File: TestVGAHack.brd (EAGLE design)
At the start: 18.3 x 7.9 mm, 0 parts

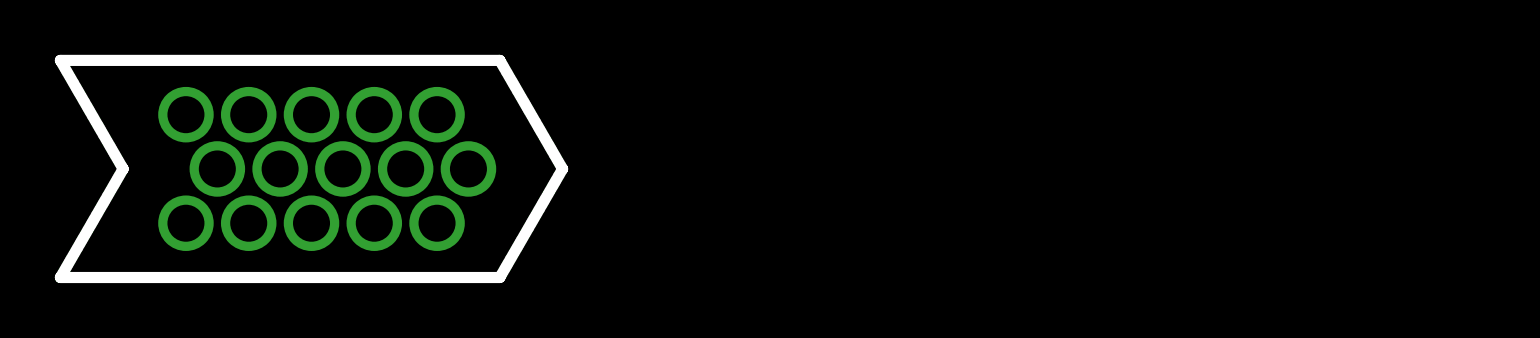
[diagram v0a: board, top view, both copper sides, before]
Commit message: Two VGA's at the same time
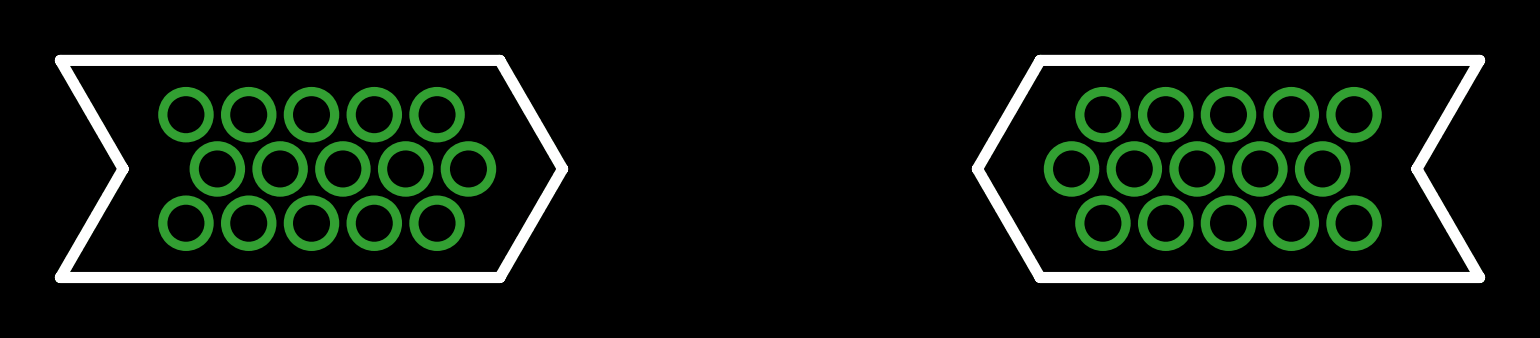
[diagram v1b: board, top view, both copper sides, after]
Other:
- board size 18.3 x 7.9 mm -> 51.8 x 7.9 mm
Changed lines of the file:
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@@
 <setting verticaltext="up"/>
 </settings>
-<grid distance="1.98" unitdist="mm" unit="mm" style="lines" multiple="1" display="yes" altdistance="1.98" altunitdist="mm" altunit="mm"/>
+<grid distance="1.145" unitdist="mm" unit="mm" style="lines" multiple="2" display="yes" altdistance="1.98" altunitdist="mm" altunit="mm"/>
 <layers>
 <layer number="1" name="Top" color="4" fill="1" visible="yes" active="yes"/>
@@
 <wire x1="-4.58" y1="1.98" x2="11.45" y2="1.98" width="0.4064" layer="20"/>
 <wire x1="-4.58" y1="-5.94" x2="11.45" y2="-5.94" width="0.4064" layer="20"/>
+<wire x1="44.9" y1="-1.98" x2="47.19" y2="-5.94" width="0.4064" layer="20"/>
+<wire x1="47.19" y1="1.98" x2="44.9" y2="-1.98" width="0.4064" layer="20"/>
+<wire x1="28.87" y1="-1.98" x2="31.16" y2="-5.94" width="0.4064" layer="20"/>
+<wire x1="31.16" y1="1.98" x2="28.87" y2="-1.98" width="0.4064" layer="20"/>
+<wire x1="47.19" y1="1.98" x2="31.16" y2="1.98" width="0.4064" layer="20"/>
+<wire x1="47.19" y1="-5.94" x2="31.16" y2="-5.94" width="0.4064" layer="20"/>
 </plain>
 <attributes>
@@
 </elements>
 <signals>
-<signal name="S$1">
+<signal name="C5">
 <via x="0" y="0" extent="1-16" drill="1.35"/>
 </signal>
-<signal name="S$2">
+<signal name="C10">
 <via x="1.145" y="-1.98" extent="1-16" drill="1.35"/>
 </signal>
-<signal name="S$3">
+<signal name="C15">
 <via x="0" y="-3.96" extent="1-16" drill="1.35"/>
 </signal>
-<signal name="S$4">
+<signal name="C4">
 <via x="2.29" y="0" extent="1-16" drill="1.35"/>
 </signal>
-<signal name="S$5">
+<signal name="C3">
 <via x="4.58" y="0" extent="1-16" drill="1.35"/>
 </signal>
-<signal name="S$6">
+<signal name="C2">
 <via x="6.87" y="0" extent="1-16" drill="1.35"/>
 </signal>
-<signal name="S$7">
+<signal name="C1">
 <via x="9.16" y="0" extent="1-16" drill="1.35"/>
 </signal>
-<signal name="S$8">
+<signal name="C14">
 <via x="2.29" y="-3.96" extent="1-16" drill="1.35"/>
 </signal>
-<signal name="S$9">
+<signal name="C13">
 <via x="4.58" y="-3.96" extent="1-16" drill="1.35"/>
 </signal>
-<signal name="S$10">
+<signal name="C12">
 <via x="6.87" y="-3.96" extent="1-16" drill="1.35"/>
 </signal>
-<signal name="S$11">
+<signal name="C11">
 <via x="9.16" y="-3.96" extent="1-16" drill="1.35"/>
 </signal>
-<signal name="S$12">
+<signal name="C9">
 <via x="3.435" y="-1.98" extent="1-16" drill="1.35"/>
 </signal>
-<signal name="S$13">
+<signal name="C8">
 <via x="5.725" y="-1.98" extent="1-16" drill="1.35"/>
 </signal>
-<signal name="S$14">
+<signal name="C7">
 <via x="8.015" y="-1.98" extent="1-16" drill="1.35"/>
 </signal>
-<signal name="S$15">
+<signal name="C6">
 <via x="10.305" y="-1.98" extent="1-16" drill="1.35"/>
 </signal>
+<signal name="C2_5">
+<via x="42.61" y="0" extent="1-16" drill="1.35"/>
+</signal>
+<signal name="C17">
+<via x="41.465" y="-1.98" extent="1-16" drill="1.35"/>
+</signal>
+<signal name="C18">
+<via x="42.61" y="-3.96" extent="1-16" drill="1.35"/>
+</signal>
+<signal name="C2_4">
+<via x="40.32" y="0" extent="1-16" drill="1.35"/>
+</signal>
+<signal name="C2_3">
+<via x="38.03" y="0" extent="1-16" drill="1.35"/>
+</signal>
+<signal name="C2_2">
+<via x="35.74" y="0" extent="1-16" drill="1.35"/>
+</signal>
+<signal name="C2_1">
+<via x="33.45" y="0" extent="1-16" drill="1.35"/>
+</signal>
+<signal name="C23">
+<via x="40.32" y="-3.96" extent="1-16" drill="1.35"/>
+</signal>
+<signal name="C24">
+<via x="38.03" y="-3.96" extent="1-16" drill="1.35"/>
+</signal>
+<signal name="C25">
+<via x="35.74" y="-3.96" extent="1-16" drill="1.35"/>
+</signal>
+<signal name="C26">
+<via x="33.45" y="-3.96" extent="1-16" drill="1.35"/>
+</signal>
+<signal name="C27">
+<via x="39.175" y="-1.98" extent="1-16" drill="1.35"/>
+</signal>
+<signal name="C2_8">
+<via x="36.885" y="-1.98" extent="1-16" drill="1.35"/>
+</signal>
+<signal name="C2_7">
+<via x="34.595" y="-1.98" extent="1-16" drill="1.35"/>
+</signal>
+<signal name="C2_6">
+<via x="32.305" y="-1.98" extent="1-16" drill="1.35"/>
+</signal>
 </signals>
